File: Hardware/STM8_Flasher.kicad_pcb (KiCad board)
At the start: 2 copper layers, 39 x 19.5 mm, 24 parts, among them J1 SWIM_PORT, J2 UART_PORT, J3 Power, J4 ISP, SW1 PROG_BUTTON, U1 STM8S003F3P, U2 AT24CS64-SSHM, U3 MIC5205-3.3

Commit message: update
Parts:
- U2: footprint Housings_SOIC:SOIC-8_3.9x4.9mm_Pitch1.27mm -> Housings_SSOP:TSSOP-8_4.4x3mm_Pitch0.65mm
- moved U2 0.50 mm to (114.5, 129.0)
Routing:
- net GND: track 46.2 -> 34.9 mm, vias 1 -> 0
- net +3V3: track 63.4 -> 65.8 mm
- net I2C_SCL: track 11.1 -> 9.94 mm
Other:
- board size 39 x 19.5 mm -> 38 x 19.5 mm
- net class Default: clearance 0.25 -> 0.2
- rule trace_clearance: 0.25 -> 0.2
- board text added: "+5V"
- board text added: "G"
- board text added: "GND"
- board text added: "ISP"
- board text added: "NRST"
- board text added: "R"
- board text added: "RX"
- board text added: "S"
- board text added: "STM8 FLASHER V1.0"
- board text added: "SWIM"
- board text added: "T"
- board text added: "TX"
- board text added: "V"

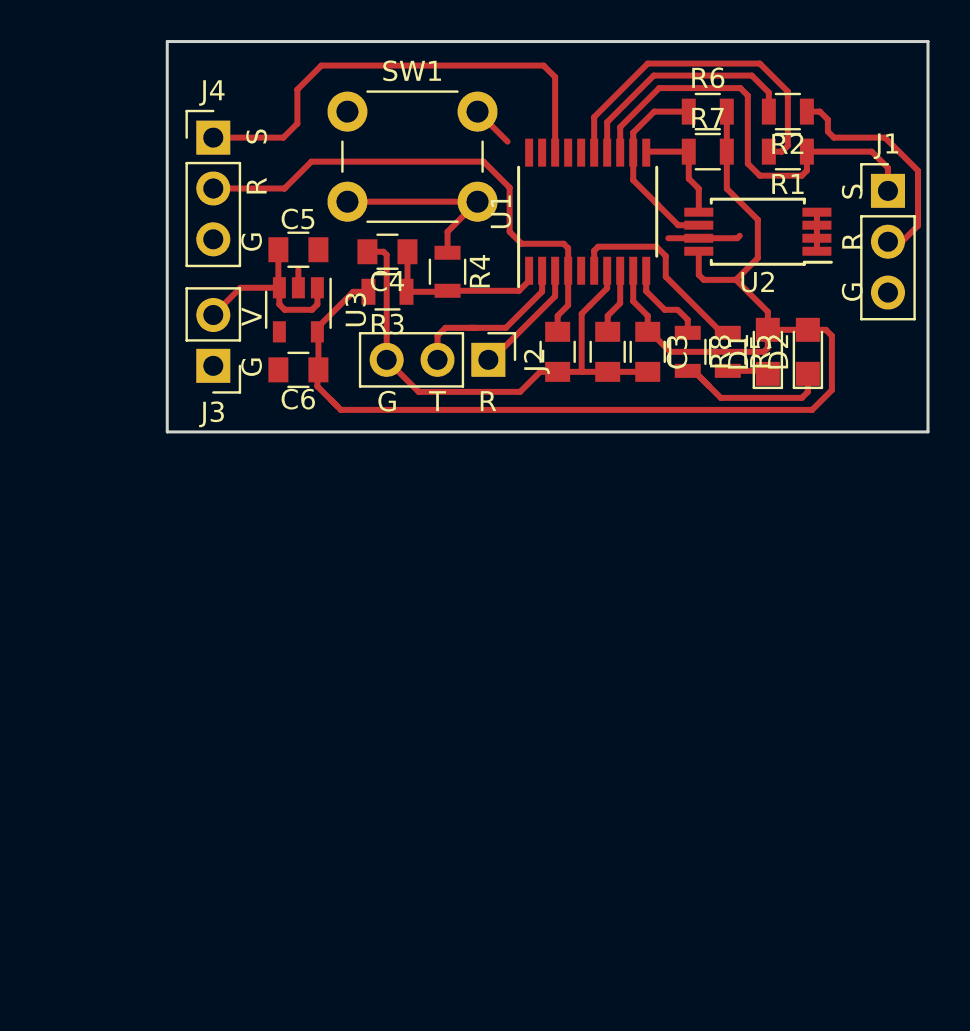
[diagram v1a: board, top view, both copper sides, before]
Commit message: schematic update
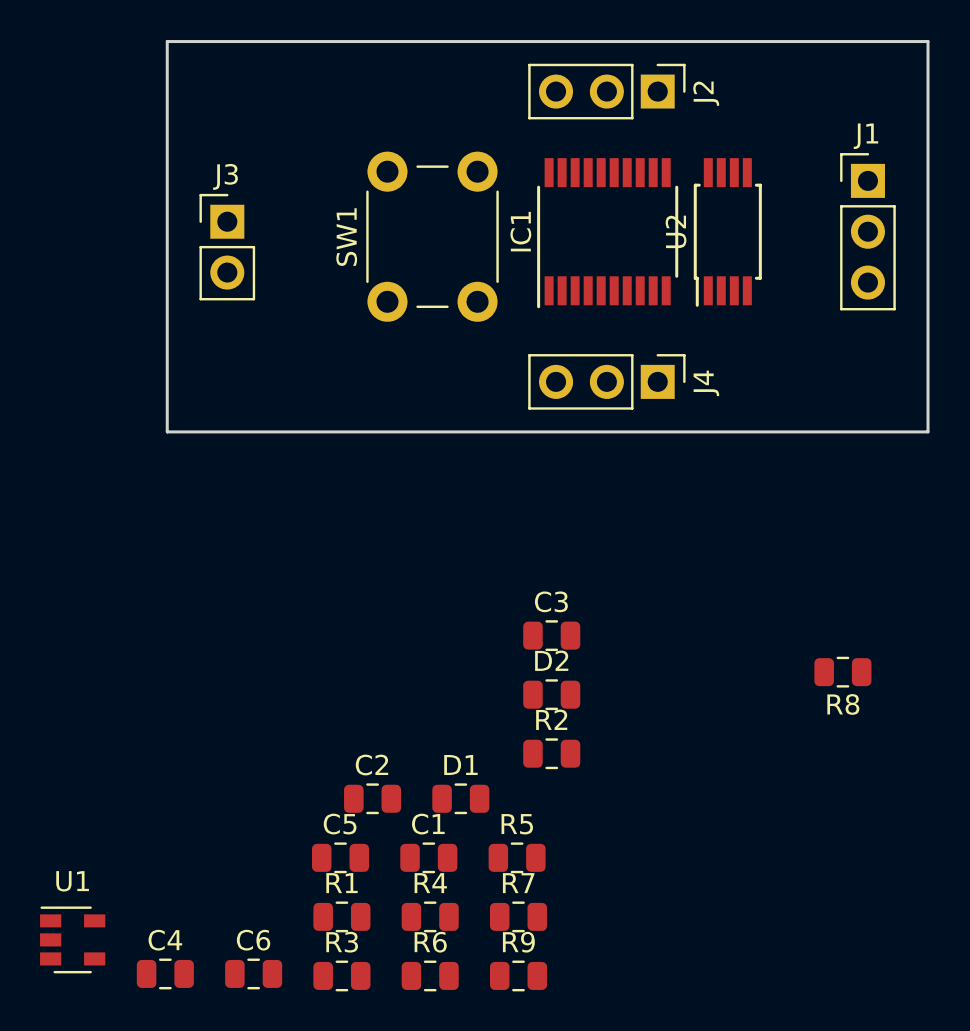
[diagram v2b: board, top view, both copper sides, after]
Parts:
- removed U3: MIC5205-3.3, TO_SOT_Packages_SMD:SOT-23-5
- added IC1: STM8S003F3P, Package_SO:TSSOP-20_4.4x6.5mm_P0.65mm, F.Cu at (107.0, 129.0)
- added R9: 1k, Resistor_SMD:R_0805_2012Metric, F.Cu at (102.5, 166.2)
- C1: value 0.1uF -> 1u; footprint Capacitors_SMD:C_0805 -> Capacitor_SMD:C_0805_2012Metric
- C2, C5: value 1uF -> 1u; footprint Capacitors_SMD:C_0805 -> Capacitor_SMD:C_0805_2012Metric
- C3: value 10uF -> 1u; footprint Capacitors_SMD:C_0805 -> Capacitor_SMD:C_0805_2012Metric
- C4: value 0.1uF -> 10u; footprint Capacitors_SMD:C_0805 -> Capacitor_SMD:C_0805_2012Metric
- C6: value 10uF -> 0.1u; footprint Capacitors_SMD:C_0805 -> Capacitor_SMD:C_0805_2012Metric
- D1, D2: footprint LEDs:LED_0805 -> Capacitor_SMD:C_0805_2012Metric
- J1: value SWIM_PORT -> UART; footprint Pin_Headers:Pin_Header_Straight_1x03_Pitch2.54mm -> Connector_PinHeader_2.54mm:PinHeader_1x03_P2.54mm_Vertical
- J2: value UART_PORT -> Conn_01x03; footprint Pin_Headers:Pin_Header_Straight_1x03_Pitch2.54mm -> Connector_PinHeader_2.54mm:PinHeader_1x03_P2.54mm_Vertical
- J3: value Power -> Conn_01x02; footprint Pin_Headers:Pin_Header_Straight_1x02_Pitch2.54mm -> Connector_PinHeader_2.54mm:PinHeader_1x02_P2.54mm_Vertical
- J4: value ISP -> UART; footprint Pin_Headers:Pin_Header_Straight_1x03_Pitch2.54mm -> Connector_PinHeader_2.54mm:PinHeader_1x03_P2.54mm_Vertical
- R1: value 680 -> 10k; footprint Resistors_SMD:R_0805 -> Resistor_SMD:R_0805_2012Metric
- R2: value 22 -> 1k; footprint Resistors_SMD:R_0805 -> Resistor_SMD:R_0805_2012Metric
- R3: value 10k -> 3.3k; footprint Resistors_SMD:R_0805 -> Resistor_SMD:R_0805_2012Metric
- R4, R7: footprint Resistors_SMD:R_0805 -> Resistor_SMD:R_0805_2012Metric
- R5: value 330 -> 100; footprint Resistors_SMD:R_0805 -> Resistor_SMD:R_0805_2012Metric
- R6: value 4.7k -> 100; footprint Resistors_SMD:R_0805 -> Resistor_SMD:R_0805_2012Metric
- R8: value 330 -> 4.7k; footprint Resistors_SMD:R_0805 -> Resistor_SMD:R_0805_2012Metric
- SW1: value PROG_BUTTON -> SW_Push; footprint Buttons_Switches_THT:SW_PUSH_6mm -> Button_Switch_THT:SW_PUSH_6mm
- U1: value STM8S003F3P -> MIC5205-3.3YM5; footprint Housings_SSOP:TSSOP-20_4.4x6.5mm_Pitch0.65mm -> Package_TO_SOT_SMD:SOT-23-5
- U2: value AT24CS64-SSHM -> 24LC256; footprint Housings_SSOP:TSSOP-8_4.4x3mm_Pitch0.65mm -> Package_SO:TSSOP-8_4.4x3mm_P0.65mm
- moved R6 45.3 mm to (98.1, 166.2)
- moved U1 44.6 mm to (80.3, 164.4), turned to 0 degrees
- moved R1 44.2 mm to (93.7, 163.2), turned to 0 degrees
- moved R7 39.4 mm to (102.5, 163.2)
- moved C4 37.7 mm to (84.9, 166.1), turned to 0 degrees
- moved R3 34.3 mm to (93.7, 166.2), turned to 0 degrees
- moved R2 34.2 mm to (104.2, 155.1), turned to 0 degrees
- moved R4 32.2 mm to (98.1, 163.2), turned to 0 degrees
- moved C5 30.4 mm to (93.7, 160.3)
- moved C6 30.3 mm to (89.3, 166.1), turned to 0 degrees
- moved R5 27.4 mm to (102.5, 160.3), turned to 0 degrees
- moved D1 27.1 mm to (99.7, 157.3), turned to 0 degrees
- moved C1 26.1 mm to (98.1, 160.3), turned to 0 degrees
- moved J4 25.3 mm to (109.5, 136.5), turned to 270 degrees
- moved C2 25.2 mm to (95.3, 157.3), turned to 0 degrees
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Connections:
- C1 pad 1: Net-(C1-Pad1) -> VCC
- C2 pad 1: Net-(C2-Pad1) -> +3V3
- C4 pad 1: PROG_SWITCH -> Net-(C4-Pad1)
- C5 pad 1: VCC -> Net-(C5-Pad1)
- C6 pad 1: +3V3 -> PROG_SWITCH
- J1 pad 1: SWIM_INT -> Net-(J1-Pad1)
- J2 pad 1: UART_RX -> Net-(IC1-Pad18)
- J2 pad 2: UART_TX -> Net-(C4-Pad1)
- J4 pad 1: Net-(J4-Pad1) -> UART_RX
- J4 pad 2: Net-(C1-Pad1) -> UART_TX
- R1 pad 1: SWIM_INT -> +3V3
- R1 pad 2: SWIM_OUT -> PROG_SWITCH
- R2 pad 1: Net-(J1-Pad2) -> Net-(R2-Pad1)
- R2 pad 2: SWIM_NRST -> PROG_SWITCH
- R3 pad 1: PROG_SWITCH -> SWIM_OUT
- R4 pad 1: Net-(R4-Pad1) -> Net-(D1-Pad1)
- R4 pad 2: PROG_SWITCH -> LED_RED
- R5 pad 1: LED_RED -> Net-(J1-Pad1)
- R5 pad 2: Net-(D1-Pad1) -> SWIM_OUT
- R6 pad 1: I2C_SCL -> SWIM_NRST
- R6 pad 2: +3V3 -> Net-(J1-Pad2)
- R7 pad 1: I2C_SDA -> +3V3
- R7 pad 2: +3V3 -> I2C_SDA
- R8 pad 1: LED_GREEN -> +3V3
- R8 pad 2: Net-(D2-Pad1) -> I2C_SCL
- SW1 pad 1: GND -> Net-(R2-Pad1)
- SW1 pad 2: Net-(R4-Pad1) -> GND
- U1 pad 1: PROG_SWITCH -> VCC
- U1 pad 2: UART_TX -> GND
- U1 pad 3: UART_RX -> VCC
- U1 pad 4: Net-(C1-Pad1) -> (no net)
- U1 pad 5: Net-(U1-Pad5) -> +3V3
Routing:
- net +3V3: track 65.8 -> 0.00 mm
- net GND: track 34.9 -> 0.00 mm
- net Net-(C1-Pad1): track 25.8 -> 0.00 mm
- net Net-(J4-Pad1): track 23.6 -> 0.00 mm
- net SWIM_INT: track 22.1 -> 0.00 mm
- net SWIM_OUT: track 17.0 -> 0.00 mm
- net SWIM_NRST: track 11.9 -> 0.00 mm
- net Net-(J1-Pad2): track 11.7 -> 0.00 mm
- net LED_RED: track 10.1 -> 0.00 mm
- net I2C_SCL: track 9.94 -> 0.00 mm
- net Net-(R4-Pad1): track 9.67 -> 0.00 mm
- net VCC: track 9.57 -> 0.00 mm
- net PROG_SWITCH: track 8.94 -> 0.00 mm
- net UART_TX: track 8.68 -> 0.00 mm
- net Net-(D2-Pad1): track 8.66 -> 0.00 mm
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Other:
- board text removed: "+5V"
- board text removed: "G"
- board text removed: "GND"
- board text removed: "ISP"
- board text removed: "NRST"
- board text removed: "R"
- board text removed: "RX"
- board text removed: "S"
- board text removed: "STM8 FLASHER V1.0"
- board text removed: "SWIM"
- board text removed: "T"
- board text removed: "TX"
- board text removed: "V"

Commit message: new schematic
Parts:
- removed C6: 0.1u, Capacitor_SMD:C_0805_2012Metric
- removed IC1: STM8S003F3P, Package_SO:TSSOP-20_4.4x6.5mm_P0.65mm
- removed R9: 1k, Resistor_SMD:R_0805_2012Metric
- added J5: SWIM_PORT4, Connector_Molex:Molex_KK-254_AE-6410-03A_1x03_P2.54mm_Vertical, F.Cu at (158.5, 67.5)
- added J6: SWIM_PORT5, Connector_Molex:Molex_KK-254_AE-6410-03A_1x03_P2.54mm_Vertical, F.Cu at (158.5, 77.5)
- added J7: ISP, Connector_PinHeader_2.54mm:PinHeader_1x03_P2.54mm_Vertical, F.Cu at (132.4, 77.9)
- added U3: 24LC256, Package_SO:TSSOP-8_4.4x3mm_P0.65mm, F.Cu at (143.0, 70.0)
- C1, C2, C3, C5: footprint Capacitor_SMD:C_0805_2012Metric -> Capacitor_SMD:C_0603_1608Metric
- C4: value 10u -> 10n; footprint Capacitor_SMD:C_0805_2012Metric -> Capacitor_SMD:C_0603_1608Metric
- D1: value LED -> RED_LED; footprint Capacitor_SMD:C_0805_2012Metric -> LED_SMD:LED_0603_1608Metric
- D2: value LED -> GREEN_LED; footprint Capacitor_SMD:C_0805_2012Metric -> LED_SMD:LED_0603_1608Metric
- J1: value UART -> PWR; footprint Connector_PinHeader_2.54mm:PinHeader_1x03_P2.54mm_Vertical -> Connector_Molex:Molex_KK-254_AE-6410-02A_1x02_P2.54mm_Vertical
- J2: value Conn_01x03 -> SWIM_PORT1; footprint Connector_PinHeader_2.54mm:PinHeader_1x03_P2.54mm_Vertical -> Connector_Molex:Molex_KK-254_AE-6410-03A_1x03_P2.54mm_Vertical
- J3: value Conn_01x02 -> SWIM_PORT2; footprint Connector_PinHeader_2.54mm:PinHeader_1x02_P2.54mm_Vertical -> Connector_Molex:Molex_KK-254_AE-6410-03A_1x03_P2.54mm_Vertical
- J4: value UART -> SWIM_PORT3; footprint Connector_PinHeader_2.54mm:PinHeader_1x03_P2.54mm_Vertical -> Connector_Molex:Molex_KK-254_AE-6410-03A_1x03_P2.54mm_Vertical
- R1, R2: footprint Resistor_SMD:R_0805_2012Metric -> Resistor_SMD:R_0603_1608Metric
- R3: value 3.3k -> 1k; footprint Resistor_SMD:R_0805_2012Metric -> Resistor_SMD:R_0603_1608Metric
- R4: value 1k -> 3.3k; footprint Resistor_SMD:R_0805_2012Metric -> Resistor_SMD:R_0603_1608Metric
- R5, R6: value 100 -> 3.3k; footprint Resistor_SMD:R_0805_2012Metric -> Resistor_SMD:R_0603_1608Metric
- R7, R8: value 4.7k -> 3.3k; footprint Resistor_SMD:R_0805_2012Metric -> Resistor_SMD:R_0603_1608Metric
- SW1: value SW_Push -> PROG_SW
- U1: value MIC5205-3.3YM5 -> STM8S003F3P; footprint Package_TO_SOT_SMD:SOT-23-5 -> Package_SO:TSSOP-20_4.4x6.5mm_P0.65mm
- U2: value 24LC256 -> MIC5205-3.3YM5; footprint Package_SO:TSSOP-8_4.4x3mm_P0.65mm -> Package_TO_SOT_SMD:SOT-23-5
- moved U1 118.4 mm to (143.0, 64.0)
- moved C4 103.7 mm to (148.3, 84.0)
- moved R3 101.0 mm to (152.3, 84.0)
- moved R6 96.4 mm to (152.3, 86.5)
- moved C2 95.0 mm to (152.4, 81.4)
- moved R1 94.2 mm to (148.3, 86.5)
- moved J3 93.2 mm to (166.0, 77.5), turned to 90 degrees
- moved J4 89.2 mm to (166.0, 67.5), turned to 90 degrees
- moved R4 85.2 mm to (144.5, 91.7)
- moved C5 85.1 mm to (140.5, 89.2)
- moved C1 84.9 mm to (144.5, 89.2)
- moved R5 84.9 mm to (148.5, 89.0)
- moved D2 83.4 mm to (148.4, 81.4)
- moved R7 80.7 mm to (144.5, 94.2)
- moved R2 70.8 mm to (140.5, 94.2)
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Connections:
- C1 pad 1: VCC -> NRST
- C2 pad 1: +3V3 -> Net-(C2-Pad1)
- C3 pad 1: +3V3 -> Net-(C3-Pad1)
- C5 pad 1: Net-(C5-Pad1) -> MCU_3.3V
- D1 pad 1: Net-(D1-Pad1) -> READ_LED
- D1 pad 2: +3V3 -> Net-(D1-Pad2)
- D2 pad 1: Net-(D2-Pad1) -> WRITE _LED
- D2 pad 2: +3V3 -> Net-(D2-Pad2)
- J1 pad 1: Net-(J1-Pad1) -> Net-(C3-Pad1)
- J1 pad 2: Net-(J1-Pad2) -> GND
- J2 pad 1: Net-(IC1-Pad18) -> SWIM_PORT1
- J2 pad 2: Net-(C4-Pad1) -> SWIM_NRST1
- J3 pad 1: GND -> SWIM_PORT2
- J3 pad 2: VCC -> SWIM_NRST2
- J4 pad 1: UART_RX -> SWIM_PORT3
- J4 pad 2: UART_TX -> SWIM_NRST3
- R1 pad 1: +3V3 -> MCU_3.3V
- R1 pad 2: PROG_SWITCH -> PROG_SW
- R2 pad 1: Net-(R2-Pad1) -> MCU_3.3V
- R2 pad 2: PROG_SWITCH -> Net-(D1-Pad2)
- R3 pad 1: SWIM_OUT -> MCU_3.3V
- R3 pad 2: +3V3 -> Net-(D2-Pad2)
- R4 pad 1: Net-(D1-Pad1) -> MCU_3.3V
- R4 pad 2: LED_RED -> SWIM_PORT1
- R5 pad 1: Net-(J1-Pad1) -> MCU_3.3V
- R5 pad 2: SWIM_OUT -> SWIM_PORT2
- R6 pad 1: SWIM_NRST -> MCU_3.3V
- R6 pad 2: Net-(J1-Pad2) -> SWIM_PORT3
- R7 pad 1: +3V3 -> MCU_3.3V
- R7 pad 2: I2C_SDA -> SWIM_PORT4
- R8 pad 1: +3V3 -> MCU_3.3V
- R8 pad 2: I2C_SCL -> SWIM_PORT5
- SW1 pad 1: Net-(R2-Pad1) -> GND
- SW1 pad 2: GND -> PROG_SW
- U1 pad 1: VCC -> SWIM_PORT3
- U1 pad 2: GND -> SWIM_PORT4
- U1 pad 3: VCC -> SWIM_PORT5
- U1 pad 4: (no net) -> NRST
- U1 pad 5: +3V3 -> READ_LED
- U2 pad 1: GND -> Net-(C3-Pad1)
- U2 pad 2: GND -> Net-(U2-Pad2)
- U2 pad 3: GND -> Net-(C3-Pad1)
- U2 pad 4: GND -> Net-(C4-Pad1)
- U2 pad 5: I2C_SDA -> MCU_3.3V
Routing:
- removed copper zone on F.Cu, net GND
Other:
- board size 38 x 19.5 mm -> 40 x 20 mm
- net class Default: trace_width 0.3 -> 0.25
- rule pad_to_mask_clearance: 0.2 -> 0.051
- rule trace_min: 0.3 -> 0.2
